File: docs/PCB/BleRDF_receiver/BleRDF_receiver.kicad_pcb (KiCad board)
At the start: 2 copper layers, 47 x 36 mm, 17 parts, among them J1 Conn_01x02, J2 Conn_01x02, J3 Conn_01x02, J5 Conn_01x09_Pin, SW2 SW_Push, SW3 SW_SPDT_312, U1 XIAO-ESP32-C6

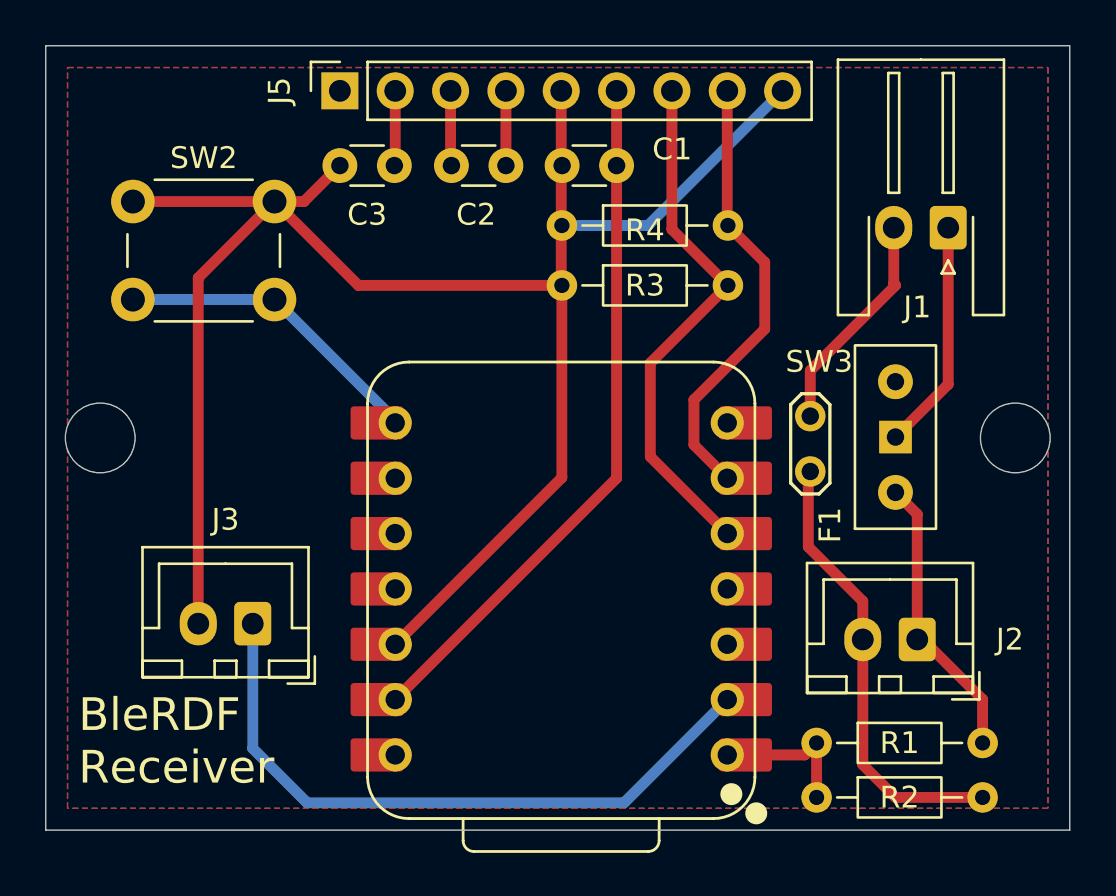
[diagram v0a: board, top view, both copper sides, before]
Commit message: Update PCB wiring and add 3D case models
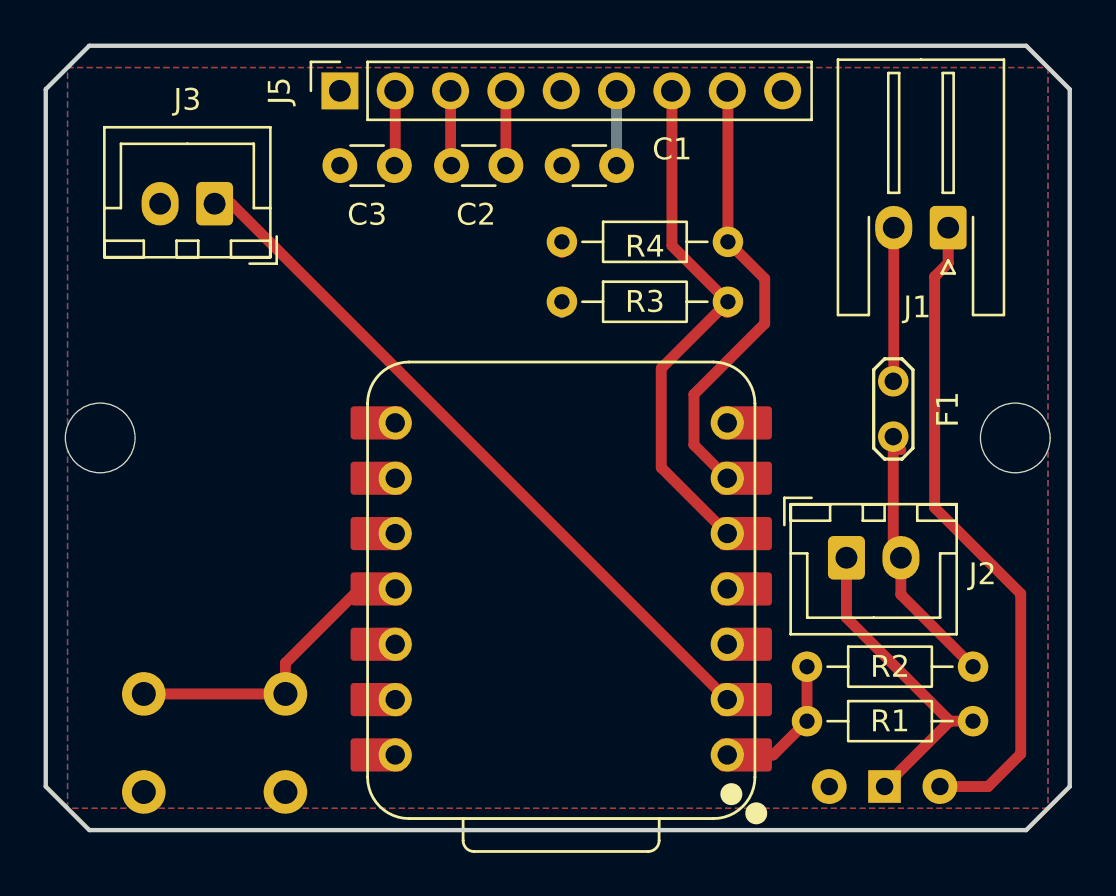
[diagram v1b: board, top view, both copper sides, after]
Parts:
- SW2, SW3: moved to B.Cu
- moved SW2 27.1 mm to (54.5, 84.2)
- moved J3 19.4 mm to (57.8, 57.2)
- moved SW3 16.0 mm to (88.5, 84.0), turned to 0 degrees
- moved R2 6.02 mm to (84.9, 78.5)
- moved J2 4.96 mm to (86.8, 73.5), turned to 0 degrees
- moved F1 4.13 mm to (88.9, 65.4)
- moved R1 1.09 mm to (84.9, 81.0)
- moved R3 0.75 mm to (73.7, 61.8)
- moved R4 0.75 mm to (73.7, 59.0)
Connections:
- J3 pad 2: VCC -> GND
- SW2 pad 1: VCC -> GND
- SW2 pad 2: Net-(U1-GPIO17/D7/RX) -> Net-(U1-GPIO18/D10/MOSI)
- SW3 pad 1: Net-(J1-Pin_1) -> Net-(J2-Pin_1)
- SW3 pad 2: Net-(J2-Pin_1) -> unconnected-(SW3-C-Pad2)
- SW3 pad 3: unconnected-(SW3-A-Pad3) -> Net-(J1-Pin_1)
- U1 pad 11: unconnected-(U1-GPIO18/D10/MOSI-Pad11) -> Net-(U1-GPIO18/D10/MOSI)
- U1 pad 8: Net-(U1-GPIO17/D7/RX) -> unconnected-(U1-GPIO17/D7/RX-Pad8)_1
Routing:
- net VCC: track 87.1 -> 0.57 mm
- net GND: track 32.1 -> 3.43 mm
- net Net-(J1-Pin_1): track 10.6 -> 30.4 mm
- net Net-(U1-GPIO17/D7/RX): track 14.5 -> 0.00 mm
- net Net-(U1-GPIO18/D10/MOSI): track 0.00 -> 14.4 mm
- net Net-(J2-Pin_2): track 20.8 -> 12.8 mm
- net Net-(J1-Pin_2): track 10.3 -> 7.06 mm
- net Net-(J3-Pin_1): track 30.5 -> 33.0 mm
- net Net-(J2-Pin_1): track 13.2 -> 14.8 mm
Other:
- outline, holes or cut-outs redrawn
- board text added: "BleRDF Receiver v1.0"
- board text removed: "BleRDF Receiver"

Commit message: Update 3D cases and pcb,hardware documentation
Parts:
- F1: footprint TestPoint:TestPoint_2Pads_Pitch2.54mm_Drill0.8mm -> Capacitor_THT:C_Disc_D4.3mm_W1.9mm_P5.00mm
- moved J2 2.87 mm to (89.4, 74.6), turned to 180 degrees
- moved F1 1.00 mm to (88.9, 64.4)
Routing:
- net Net-(J2-Pin_2): track 12.8 -> 16.7 mm
- net Net-(J1-Pin_2): track 7.06 -> 6.09 mm
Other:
- board text added: "BleRDF Receiver V1.0"
- board text removed: "BleRDF Receiver v1.0"
